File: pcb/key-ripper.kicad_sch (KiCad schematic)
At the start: 12 parts, among them SW1 ESC, SW2 TILDE, SW3 TAB, SW4 CAPS, SW5 L_SHIFT, SW6 L_CTRL

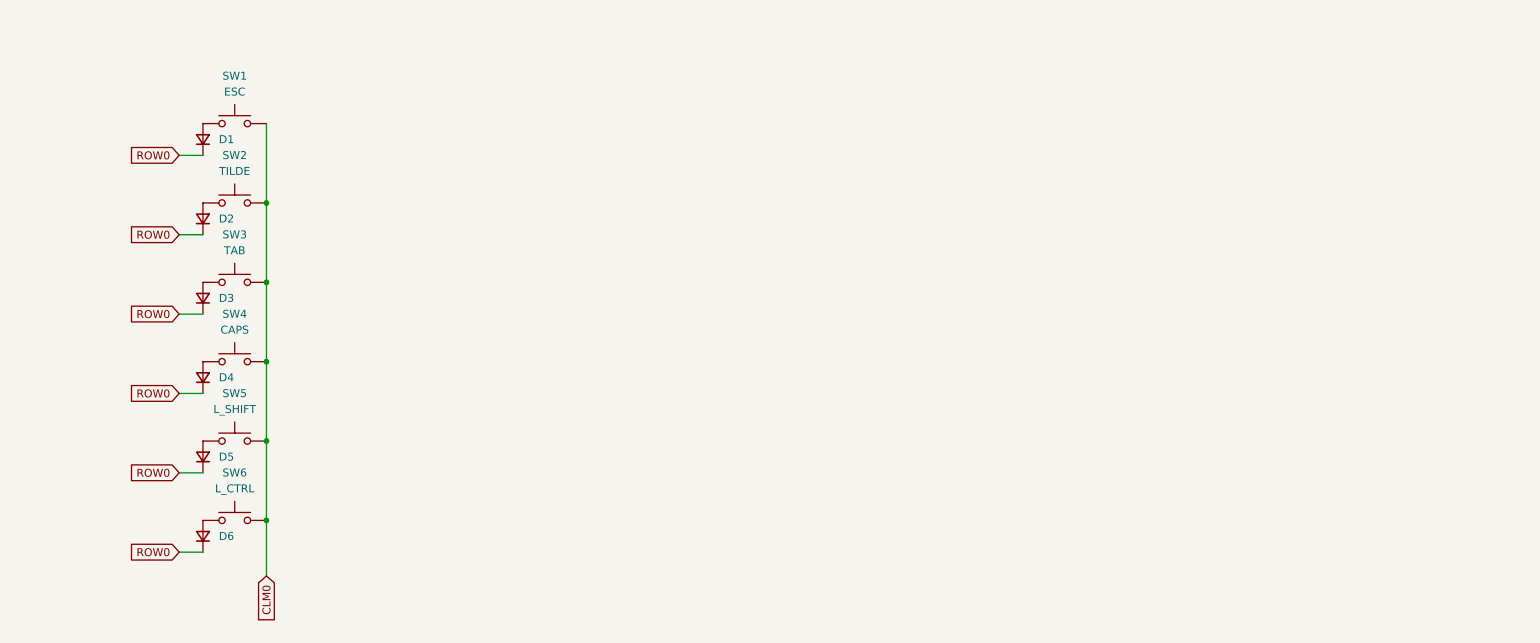
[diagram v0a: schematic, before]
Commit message: Add the keyboard matrix circuit
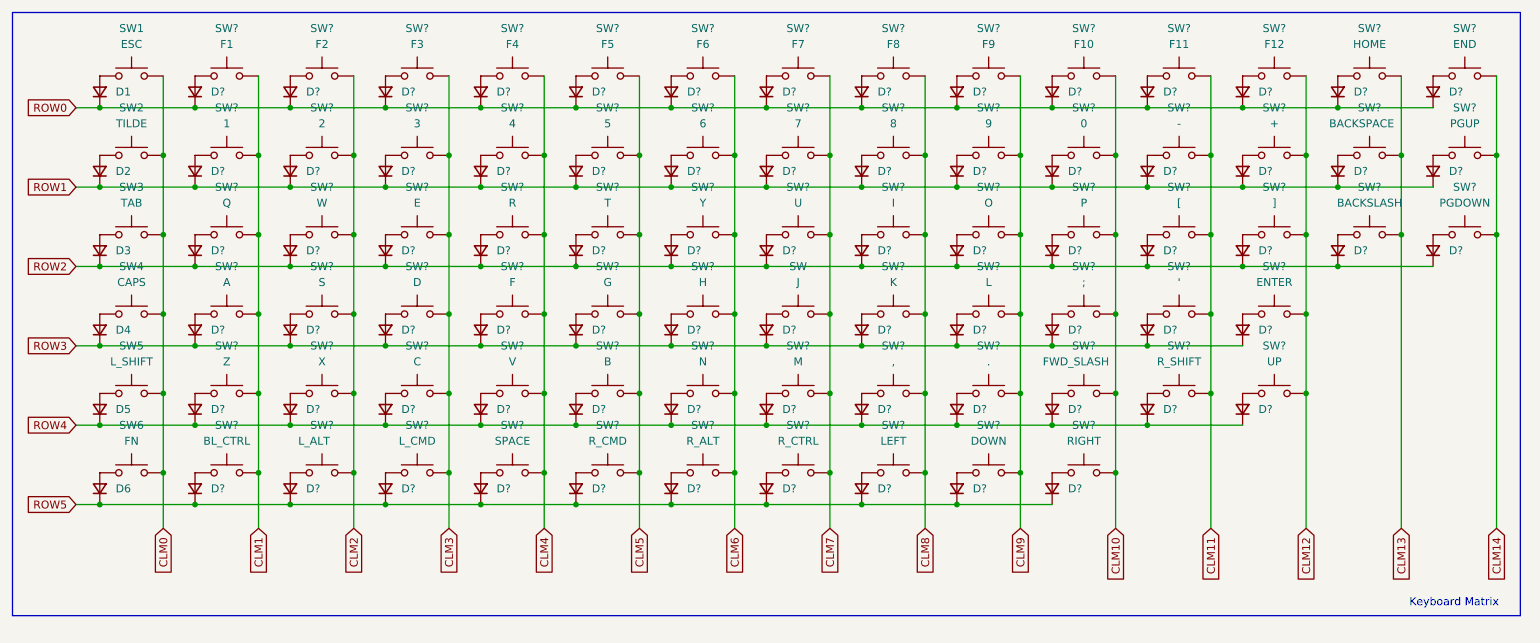
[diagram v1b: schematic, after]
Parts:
- added D? (x76): D_Small, symbol Device:D_Small
- added SW: J, Switch_Keyboard_Hotswap_Kailh:SW_Hotswap_Kailh_MX_2.00u, symbol Switch:SW_Push
- added SW?: UP, Switch_Keyboard_Hotswap_Kailh:SW_Hotswap_Kailh_MX_2.25u, symbol Switch:SW_Push
- added SW?: BL_CTRL, Switch_Keyboard_Hotswap_Kailh:SW_Hotswap_Kailh_MX_1.25u, symbol Switch:SW_Push
- added SW?: 7, Switch_Keyboard_Hotswap_Kailh:SW_Hotswap_Kailh_MX_1.00u, symbol Switch:SW_Push
- added SW?: T, Switch_Keyboard_Hotswap_Kailh:SW_Hotswap_Kailh_MX_1.50u, symbol Switch:SW_Push
- added SW?: 0, Switch_Keyboard_Hotswap_Kailh:SW_Hotswap_Kailh_MX_1.00u, symbol Switch:SW_Push
- added SW?: F2, Switch_Keyboard_Hotswap_Kailh:SW_Hotswap_Kailh_MX_1.00u, symbol Switch:SW_Push
- added SW?: 6, Switch_Keyboard_Hotswap_Kailh:SW_Hotswap_Kailh_MX_1.00u, symbol Switch:SW_Push
- added SW?: 9, Switch_Keyboard_Hotswap_Kailh:SW_Hotswap_Kailh_MX_1.00u, symbol Switch:SW_Push
- added SW?: C, Switch_Keyboard_Hotswap_Kailh:SW_Hotswap_Kailh_MX_2.25u, symbol Switch:SW_Push
- added SW?: ENTER, Switch_Keyboard_Hotswap_Kailh:SW_Hotswap_Kailh_MX_2.00u, symbol Switch:SW_Push
- added SW?: HOME, Switch_Keyboard_Hotswap_Kailh:SW_Hotswap_Kailh_MX_1.00u, symbol Switch:SW_Push
- added SW?: L_ALT, Switch_Keyboard_Hotswap_Kailh:SW_Hotswap_Kailh_MX_1.25u, symbol Switch:SW_Push
- added SW?: N, Switch_Keyboard_Hotswap_Kailh:SW_Hotswap_Kailh_MX_2.25u, symbol Switch:SW_Push
- added SW?: SPACE, Switch_Keyboard_Hotswap_Kailh:SW_Hotswap_Kailh_MX_1.25u, symbol Switch:SW_Push
- added SW?: F11, Switch_Keyboard_Hotswap_Kailh:SW_Hotswap_Kailh_MX_1.00u, symbol Switch:SW_Push
- added SW?: X, Switch_Keyboard_Hotswap_Kailh:SW_Hotswap_Kailh_MX_2.25u, symbol Switch:SW_Push
- added SW?: R_SHIFT, Switch_Keyboard_Hotswap_Kailh:SW_Hotswap_Kailh_MX_2.25u, symbol Switch:SW_Push
- added SW?: Z, Switch_Keyboard_Hotswap_Kailh:SW_Hotswap_Kailh_MX_2.25u, symbol Switch:SW_Push
- added SW?: V, Switch_Keyboard_Hotswap_Kailh:SW_Hotswap_Kailh_MX_2.25u, symbol Switch:SW_Push
- added SW?: DOWN, Switch_Keyboard_Hotswap_Kailh:SW_Hotswap_Kailh_MX_1.25u, symbol Switch:SW_Push
- added SW?: ', Switch_Keyboard_Hotswap_Kailh:SW_Hotswap_Kailh_MX_2.00u, symbol Switch:SW_Push
- added SW?: F5, Switch_Keyboard_Hotswap_Kailh:SW_Hotswap_Kailh_MX_1.00u, symbol Switch:SW_Push
- added SW?: I, Switch_Keyboard_Hotswap_Kailh:SW_Hotswap_Kailh_MX_1.50u, symbol Switch:SW_Push
- added SW?: A, Switch_Keyboard_Hotswap_Kailh:SW_Hotswap_Kailh_MX_2.00u, symbol Switch:SW_Push
- added SW?: R_CTRL, Switch_Keyboard_Hotswap_Kailh:SW_Hotswap_Kailh_MX_1.25u, symbol Switch:SW_Push
- added SW?: ,, Switch_Keyboard_Hotswap_Kailh:SW_Hotswap_Kailh_MX_2.25u, symbol Switch:SW_Push
- added SW?: 2, Switch_Keyboard_Hotswap_Kailh:SW_Hotswap_Kailh_MX_1.00u, symbol Switch:SW_Push
- added SW?: PGUP, Switch_Keyboard_Hotswap_Kailh:SW_Hotswap_Kailh_MX_1.00u, symbol Switch:SW_Push
- added SW?: F12, Switch_Keyboard_Hotswap_Kailh:SW_Hotswap_Kailh_MX_1.00u, symbol Switch:SW_Push
- added SW?: PGDOWN, Switch_Keyboard_Hotswap_Kailh:SW_Hotswap_Kailh_MX_1.50u, symbol Switch:SW_Push
- added SW?: BACKSPACE, Switch_Keyboard_Hotswap_Kailh:SW_Hotswap_Kailh_MX_1.00u, symbol Switch:SW_Push
- added SW?: F4, Switch_Keyboard_Hotswap_Kailh:SW_Hotswap_Kailh_MX_1.00u, symbol Switch:SW_Push
- added SW?: F10, Switch_Keyboard_Hotswap_Kailh:SW_Hotswap_Kailh_MX_1.00u, symbol Switch:SW_Push
- added SW?: 4, Switch_Keyboard_Hotswap_Kailh:SW_Hotswap_Kailh_MX_1.00u, symbol Switch:SW_Push
- added SW?: ., Switch_Keyboard_Hotswap_Kailh:SW_Hotswap_Kailh_MX_2.25u, symbol Switch:SW_Push
- added SW?: ;, Switch_Keyboard_Hotswap_Kailh:SW_Hotswap_Kailh_MX_2.00u, symbol Switch:SW_Push
- added SW?: 5, Switch_Keyboard_Hotswap_Kailh:SW_Hotswap_Kailh_MX_1.00u, symbol Switch:SW_Push
- added SW?: F1, Switch_Keyboard_Hotswap_Kailh:SW_Hotswap_Kailh_MX_1.00u, symbol Switch:SW_Push
- added SW?: BACKSLASH, Switch_Keyboard_Hotswap_Kailh:SW_Hotswap_Kailh_MX_1.50u, symbol Switch:SW_Push
- added SW?: U, Switch_Keyboard_Hotswap_Kailh:SW_Hotswap_Kailh_MX_1.50u, symbol Switch:SW_Push
- added SW?: R, Switch_Keyboard_Hotswap_Kailh:SW_Hotswap_Kailh_MX_1.50u, symbol Switch:SW_Push
- added SW?: R_ALT, Switch_Keyboard_Hotswap_Kailh:SW_Hotswap_Kailh_MX_1.25u, symbol Switch:SW_Push
- added SW?: F7, Switch_Keyboard_Hotswap_Kailh:SW_Hotswap_Kailh_MX_1.00u, symbol Switch:SW_Push
- added SW?: F, Switch_Keyboard_Hotswap_Kailh:SW_Hotswap_Kailh_MX_2.00u, symbol Switch:SW_Push
- added SW?: S, Switch_Keyboard_Hotswap_Kailh:SW_Hotswap_Kailh_MX_2.00u, symbol Switch:SW_Push
- added SW?: R_CMD, Switch_Keyboard_Hotswap_Kailh:SW_Hotswap_Kailh_MX_1.25u, symbol Switch:SW_Push
- added SW?: FWD_SLASH, Switch_Keyboard_Hotswap_Kailh:SW_Hotswap_Kailh_MX_2.25u, symbol Switch:SW_Push
- added SW?: +, Switch_Keyboard_Hotswap_Kailh:SW_Hotswap_Kailh_MX_1.00u, symbol Switch:SW_Push
- added SW?: G, Switch_Keyboard_Hotswap_Kailh:SW_Hotswap_Kailh_MX_2.00u, symbol Switch:SW_Push
- added SW?: 1, Switch_Keyboard_Hotswap_Kailh:SW_Hotswap_Kailh_MX_1.00u, symbol Switch:SW_Push
- added SW?: LEFT, Switch_Keyboard_Hotswap_Kailh:SW_Hotswap_Kailh_MX_1.25u, symbol Switch:SW_Push
- added SW?: 3, Switch_Keyboard_Hotswap_Kailh:SW_Hotswap_Kailh_MX_1.00u, symbol Switch:SW_Push
- added SW?: E, Switch_Keyboard_Hotswap_Kailh:SW_Hotswap_Kailh_MX_1.50u, symbol Switch:SW_Push
- added SW?: RIGHT, Switch_Keyboard_Hotswap_Kailh:SW_Hotswap_Kailh_MX_1.25u, symbol Switch:SW_Push
- added SW?: Y, Switch_Keyboard_Hotswap_Kailh:SW_Hotswap_Kailh_MX_1.50u, symbol Switch:SW_Push
- added SW?: W, Switch_Keyboard_Hotswap_Kailh:SW_Hotswap_Kailh_MX_1.50u, symbol Switch:SW_Push
- added SW?: F3, Switch_Keyboard_Hotswap_Kailh:SW_Hotswap_Kailh_MX_1.00u, symbol Switch:SW_Push
- added SW?: K, Switch_Keyboard_Hotswap_Kailh:SW_Hotswap_Kailh_MX_2.00u, symbol Switch:SW_Push
- added SW?: L, Switch_Keyboard_Hotswap_Kailh:SW_Hotswap_Kailh_MX_2.00u, symbol Switch:SW_Push
- added SW?: H, Switch_Keyboard_Hotswap_Kailh:SW_Hotswap_Kailh_MX_2.00u, symbol Switch:SW_Push
- added SW?: D, Switch_Keyboard_Hotswap_Kailh:SW_Hotswap_Kailh_MX_2.00u, symbol Switch:SW_Push
- added SW?: M, Switch_Keyboard_Hotswap_Kailh:SW_Hotswap_Kailh_MX_2.25u, symbol Switch:SW_Push
- added SW?: P, Switch_Keyboard_Hotswap_Kailh:SW_Hotswap_Kailh_MX_1.50u, symbol Switch:SW_Push
- added SW?: ], Switch_Keyboard_Hotswap_Kailh:SW_Hotswap_Kailh_MX_1.50u, symbol Switch:SW_Push
- added SW?: L_CMD, Switch_Keyboard_Hotswap_Kailh:SW_Hotswap_Kailh_MX_1.25u, symbol Switch:SW_Push
- added SW?: END, Switch_Keyboard_Hotswap_Kailh:SW_Hotswap_Kailh_MX_1.00u, symbol Switch:SW_Push
- added SW?: 8, Switch_Keyboard_Hotswap_Kailh:SW_Hotswap_Kailh_MX_1.00u, symbol Switch:SW_Push
- added SW?: F8, Switch_Keyboard_Hotswap_Kailh:SW_Hotswap_Kailh_MX_1.00u, symbol Switch:SW_Push
- added SW?: F9, Switch_Keyboard_Hotswap_Kailh:SW_Hotswap_Kailh_MX_1.00u, symbol Switch:SW_Push
- added SW?: -, Switch_Keyboard_Hotswap_Kailh:SW_Hotswap_Kailh_MX_1.00u, symbol Switch:SW_Push
- added SW?: Q, Switch_Keyboard_Hotswap_Kailh:SW_Hotswap_Kailh_MX_1.50u, symbol Switch:SW_Push
- added SW?: B, Switch_Keyboard_Hotswap_Kailh:SW_Hotswap_Kailh_MX_2.25u, symbol Switch:SW_Push
- added SW?: O, Switch_Keyboard_Hotswap_Kailh:SW_Hotswap_Kailh_MX_1.50u, symbol Switch:SW_Push
- added SW?: [, Switch_Keyboard_Hotswap_Kailh:SW_Hotswap_Kailh_MX_1.50u, symbol Switch:SW_Push
- added SW?: F6, Switch_Keyboard_Hotswap_Kailh:SW_Hotswap_Kailh_MX_1.00u, symbol Switch:SW_Push
- SW6: value L_CTRL -> FN
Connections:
- net ROW0: now also D?.1 (K), D?.1 (K), D?.1 (K), D?.1 (K), D?.1 (K), D?.1 (K), D?.1 (K), D?.1 (K), D?.1 (K), D?.1 (K), D?.1 (K), D?.1 (K), D?.1 (K), D?.1 (K); no longer D2.1 (K), D3.1 (K), D4.1 (K), D5.1 (K), D6.1 (K)
- new net: D?.2 (A), SW?.1 (x75)
- new net: D?.2 (A), SW.1
- new net CLM1: SW?.2, SW?.2, SW?.2, SW?.2, SW?.2, SW?.2
- new net CLM10: SW?.2, SW?.2, SW?.2, SW?.2, SW?.2, SW?.2
- new net CLM11: SW?.2, SW?.2, SW?.2, SW?.2, SW?.2
- new net CLM12: SW?.2, SW?.2, SW?.2, SW?.2, SW?.2
- new net CLM13: SW?.2, SW?.2, SW?.2
- new net CLM14: SW?.2, SW?.2, SW?.2
- new net CLM2: SW?.2, SW?.2, SW?.2, SW?.2, SW?.2, SW?.2
- new net CLM3: SW?.2, SW?.2, SW?.2, SW?.2, SW?.2, SW?.2
- new net CLM4: SW?.2, SW?.2, SW?.2, SW?.2, SW?.2, SW?.2
- new net CLM5: SW?.2, SW?.2, SW?.2, SW?.2, SW?.2, SW?.2
- new net CLM6: SW?.2, SW?.2, SW?.2, SW?.2, SW?.2, SW?.2
- new net CLM7: SW.2, SW?.2, SW?.2, SW?.2, SW?.2, SW?.2
- new net CLM8: SW?.2, SW?.2, SW?.2, SW?.2, SW?.2, SW?.2
- new net CLM9: SW?.2, SW?.2, SW?.2, SW?.2, SW?.2, SW?.2
- new net ROW1: D2.1 (K), D?.1 (K), D?.1 (K), D?.1 (K), D?.1 (K), D?.1 (K), D?.1 (K), D?.1 (K), D?.1 (K), D?.1 (K), D?.1 (K), D?.1 (K), D?.1 (K), D?.1 (K), D?.1 (K)
- new net ROW2: D3.1 (K), D?.1 (K), D?.1 (K), D?.1 (K), D?.1 (K), D?.1 (K), D?.1 (K), D?.1 (K), D?.1 (K), D?.1 (K), D?.1 (K), D?.1 (K), D?.1 (K), D?.1 (K), D?.1 (K)
- new net ROW3: D4.1 (K), D?.1 (K), D?.1 (K), D?.1 (K), D?.1 (K), D?.1 (K), D?.1 (K), D?.1 (K), D?.1 (K), D?.1 (K), D?.1 (K), D?.1 (K), D?.1 (K)
- new net ROW4: D5.1 (K), D?.1 (K), D?.1 (K), D?.1 (K), D?.1 (K), D?.1 (K), D?.1 (K), D?.1 (K), D?.1 (K), D?.1 (K), D?.1 (K), D?.1 (K), D?.1 (K)
- new net ROW5: D6.1 (K), D?.1 (K), D?.1 (K), D?.1 (K), D?.1 (K), D?.1 (K), D?.1 (K), D?.1 (K), D?.1 (K), D?.1 (K), D?.1 (K)
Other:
- note added: "Keyboard Matrix"
- moved on the sheet: D1, D2, D3, D4, D5, D6, SW1, SW2, SW3, SW4, SW5, SW6

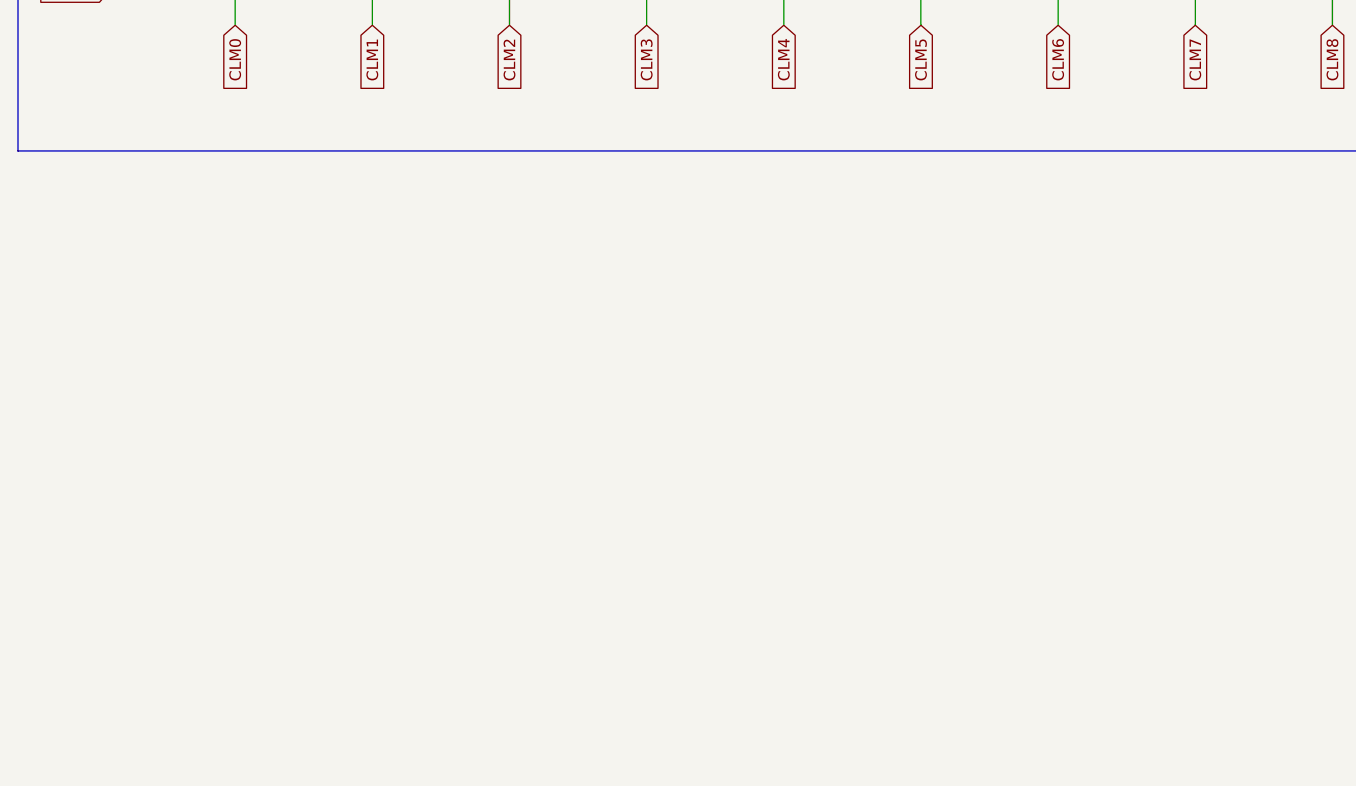
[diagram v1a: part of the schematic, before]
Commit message: Add USB connector and voltage regulator
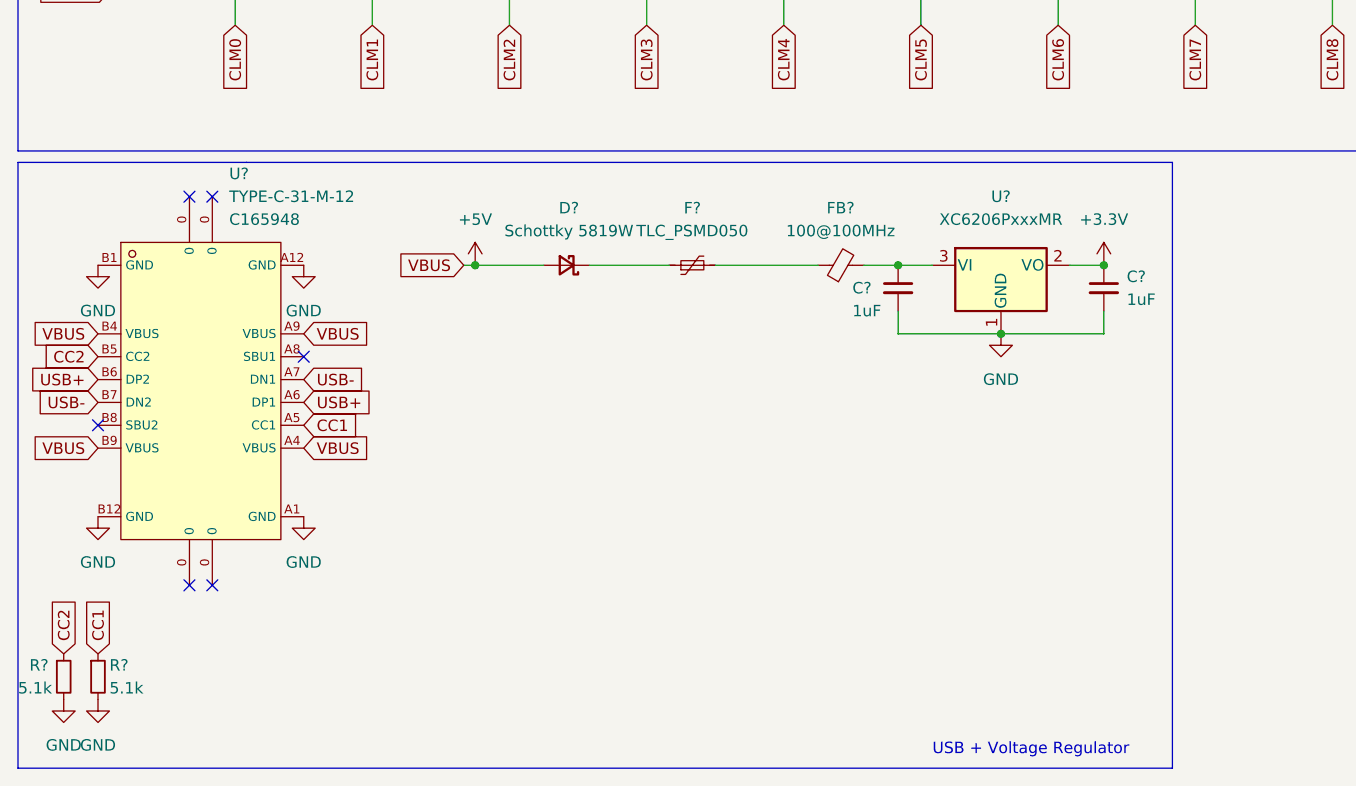
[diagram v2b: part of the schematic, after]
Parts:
- added C? (x2): 1uF, symbol Device:C_Small
- added D?: Schottky 5819W, symbol Device:D_Schottky_Small
- added F?: TLC_PSMD050, symbol Device:Polyfuse_Small
- added FB?: 100@100MHz, symbol Device:FerriteBead_Small
- added R? (x2): 5.1k, symbol Device:R_Small
- added U?: TYPE-C-31-M-12, footprint:USB-C_SMD-TYPE-C-31-M-12, symbol simple-usb-c:TYPE-C-31-M-12
- added U?: XC6206PxxxMR, Package_TO_SOT_SMD:SOT-23, symbol Regulator_Linear:XC6206PxxxMR
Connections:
- new net: C?.1, FB?.2, U?.3 (VI)
- new net: D?.1 (K), F?.1
- new net: F?.2, FB?.1
- new net +3V3: C?.1, U?.2 (VO)
- new net +5V: D?.2 (A), U?.A4 (VBUS), U?.A9 (VBUS), U?.B4 (VBUS), U?.B9 (VBUS)
- new net CC1: R?.1, U?.A5 (CC1)
- new net CC2: R?.1, U?.B5 (CC2)
- new net GND: C?.2, C?.2, R?.2, R?.2, U?.1 (GND), U?.A1 (GND), U?.A12 (GND), U?.B1 (GND), U?.B12 (GND)
- new net USB+: U?.A6 (DP1), U?.B6 (DP2)
- new net USB-: U?.A7 (DN1), U?.B7 (DN2)
- no-connect marks 0 -> 6
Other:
- note added: "USB + Voltage Regulator"

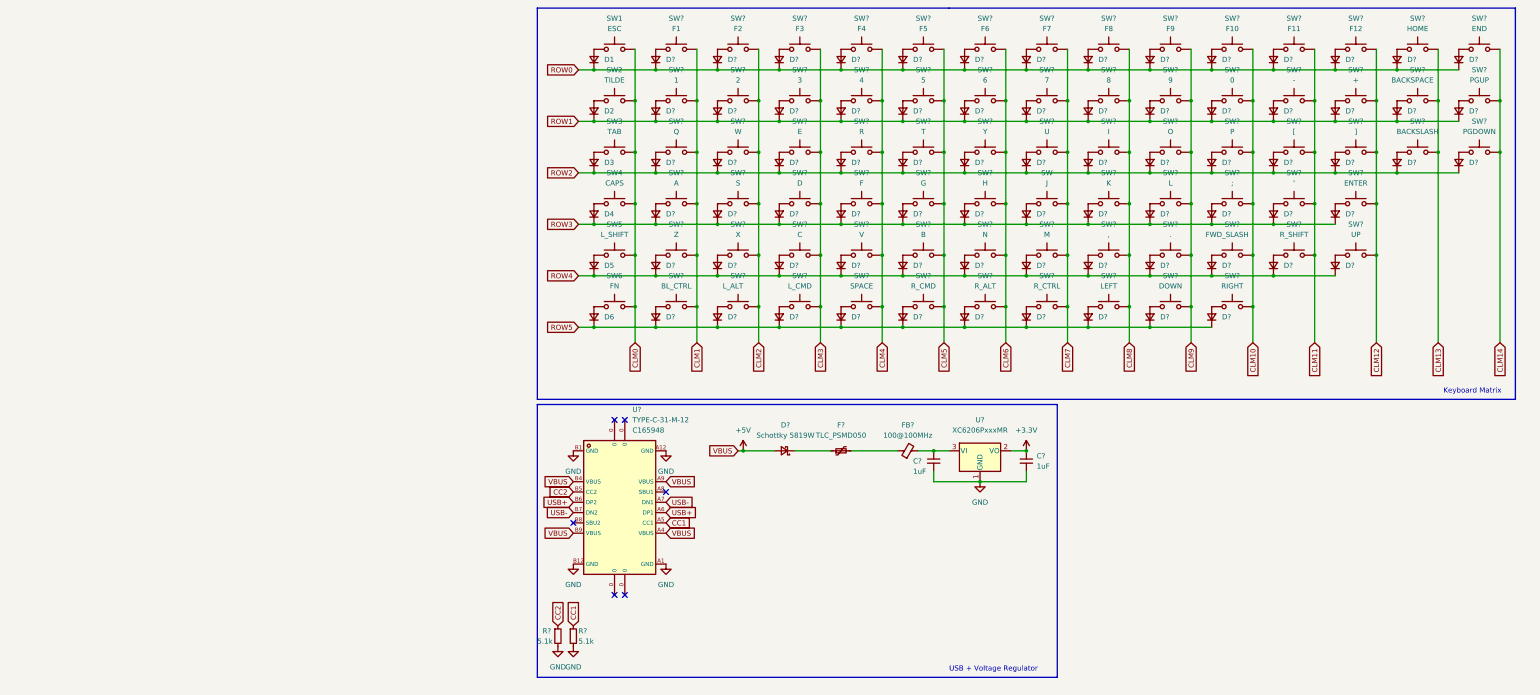
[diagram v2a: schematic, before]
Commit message: Add RP2040 and connect basic power pins
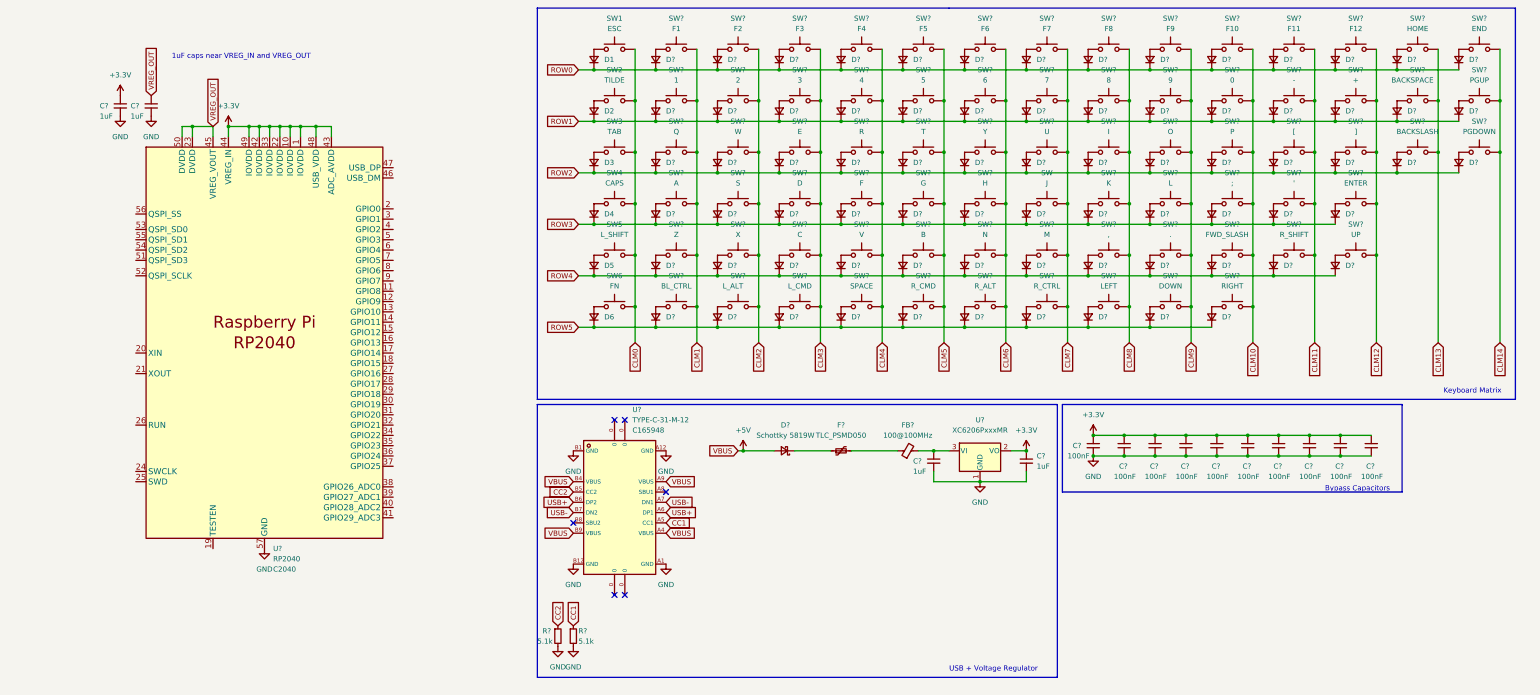
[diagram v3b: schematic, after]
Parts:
- added C? (x10): 100nF, symbol Device:C_Small
- added C? (x2): 1uF, symbol Device:C_Small
- added U?: RP2040, footprint:LQFN-56_L7.0-W7.0-P0.4-EP, symbol rp2040:RP2040
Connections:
- net +3V3: now also C?.1, C?.1, C?.1, C?.1, C?.1, C?.1, C?.1, C?.1, C?.1, C?.1, C?.1, U?.1 (IOVDD), U?.10 (IOVDD), U?.22 (IOVDD), U?.33 (IOVDD), U?.42 (IOVDD), U?.43 (ADC_AVDD), U?.44 (VREG_IN), U?.48 (USB_VDD), U?.49 (IOVDD)
- net GND: now also C?.2, C?.2, C?.2, C?.2, C?.2, C?.2, C?.2, C?.2, C?.2, C?.2, C?.2, C?.2, U?.57 (GND)
- new net VREG_OUT: C?.1, U?.23 (DVDD), U?.45 (VREG_VOUT), U?.50 (DVDD)
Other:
- note added: "1uF caps near VREG_IN and VREG_OUT"
- note added: "Bypass Capacitors"
